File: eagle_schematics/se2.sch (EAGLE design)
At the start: 2 parts

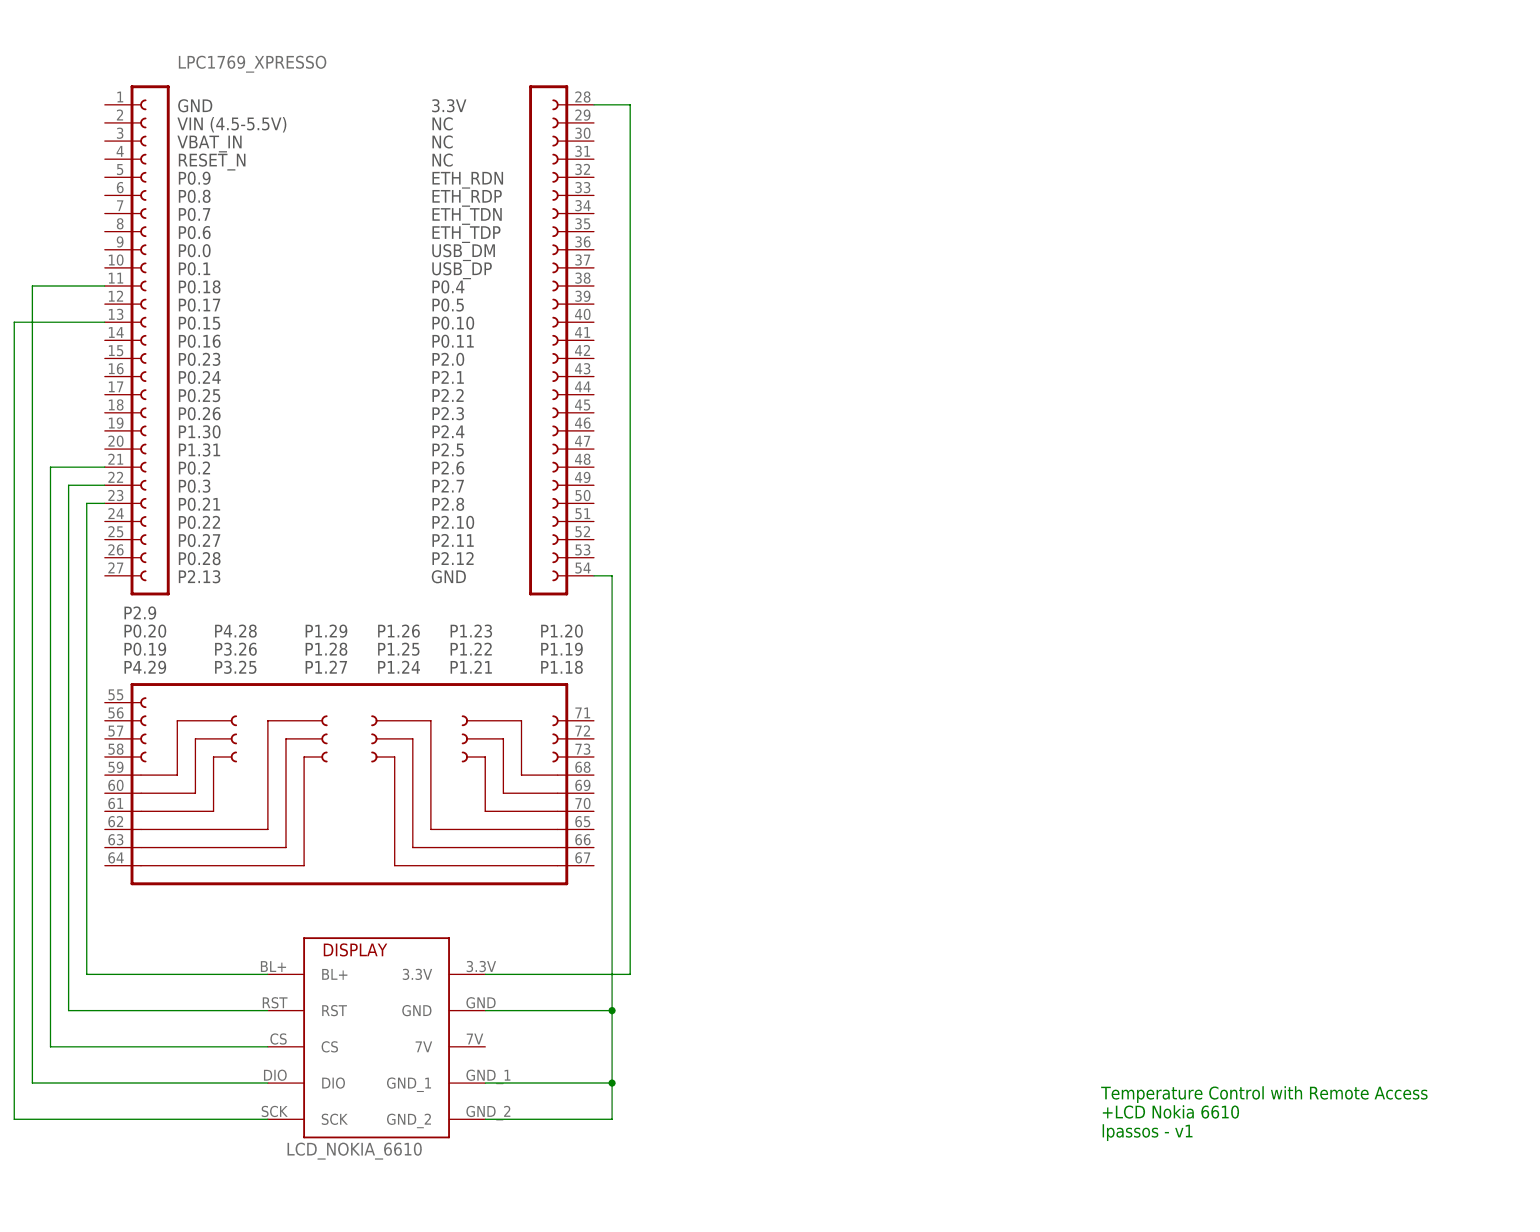
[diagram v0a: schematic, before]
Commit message: Thermometer added
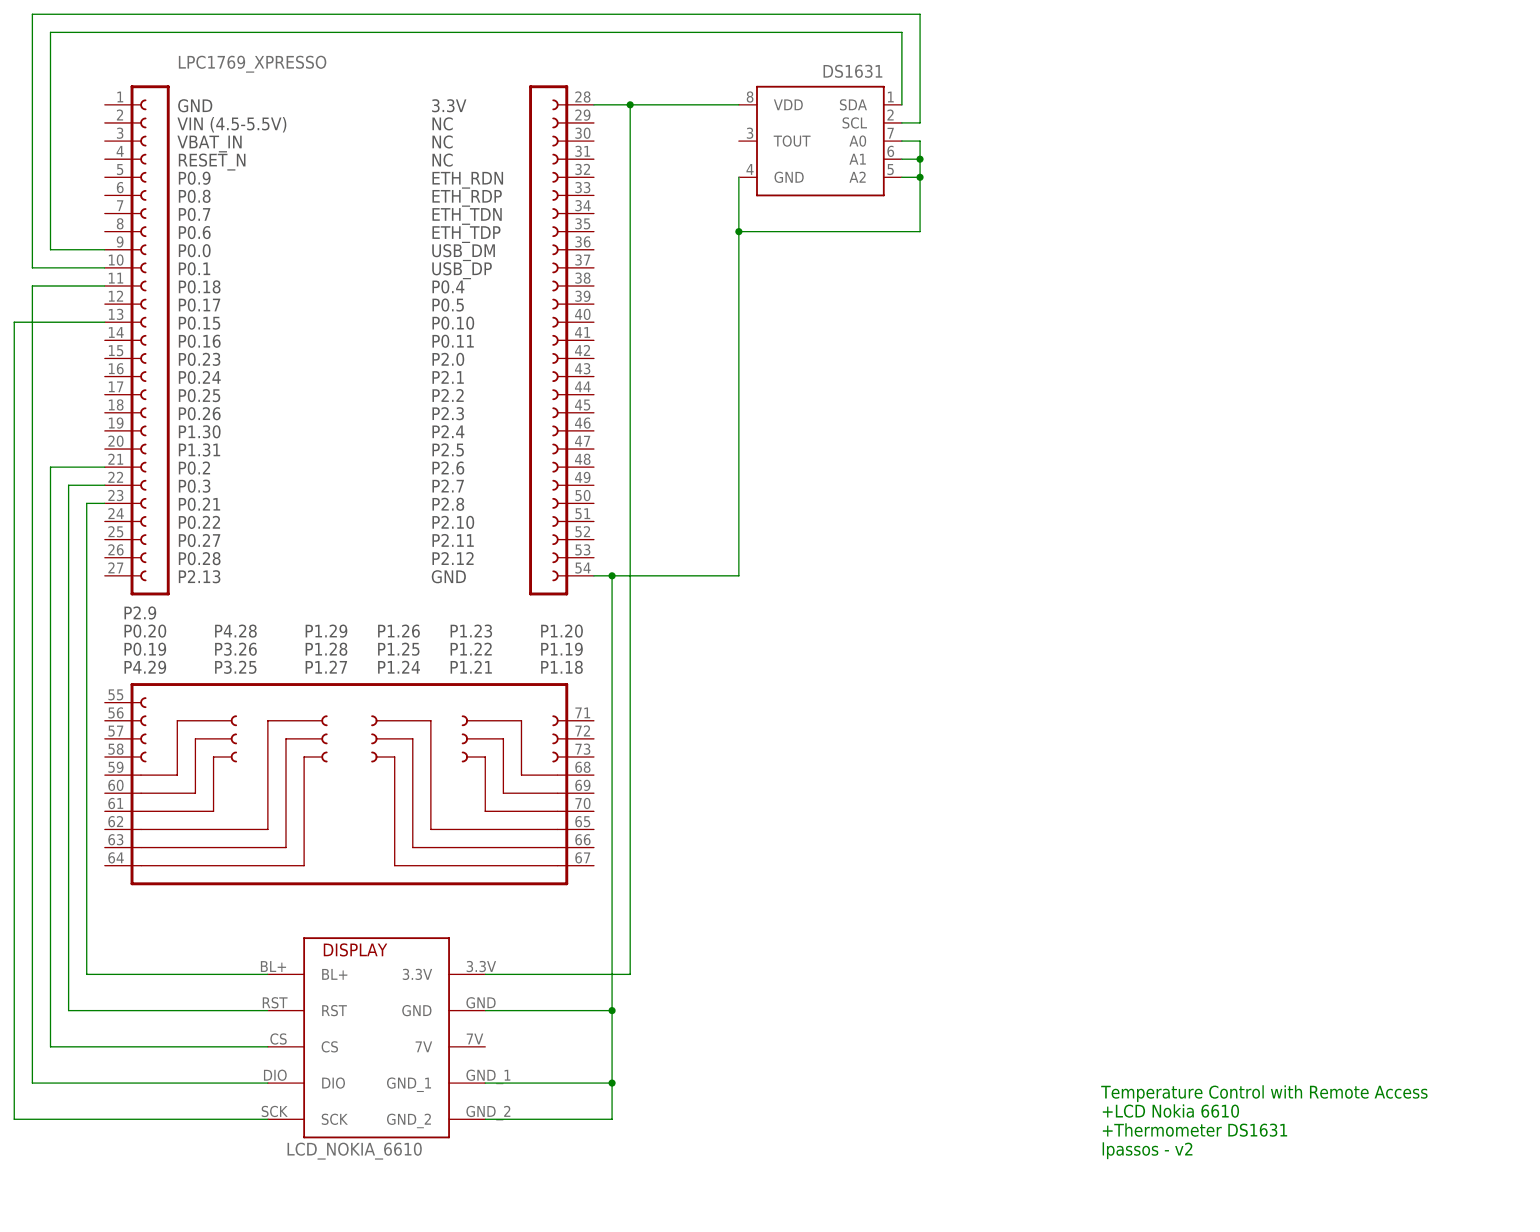
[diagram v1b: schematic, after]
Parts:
- added DS1631: DS1621, maxim:DS1621
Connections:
- removed net N$1: DISPLAY.GND, DISPLAY.GND_1, DISPLAY.GND_2, LPC1769_XPRESSO.54
- new net N$10: DS1631.SDA, LPC1769_XPRESSO.9
- new net N$11: DS1631.SCL, LPC1769_XPRESSO.10
- new net N$9: DISPLAY.GND, DISPLAY.GND_1, DISPLAY.GND_2, DS1631.A0, DS1631.A1, DS1631.A2, DS1631.GND, LPC1769_XPRESSO.54
- net N$3: now also DS1631.VDD
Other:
- note added: "Temperature Control with Remote Access +LCD Nokia 6610 +Thermometer DS1631 lpassos - v2"
- note removed: "Temperature Control with Remote Access +LCD Nokia 6610 lpassos - v1"
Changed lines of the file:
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@@
 <setting verticaltext="up"/>
 </settings>
-<grid distance="0.1" unitdist="inch" unit="inch" style="lines" multiple="1" display="no" altdistance="0.01" altunitdist="inch" altunit="inch"/>
+<grid distance="0.1" unitdist="inch" unit="inch" style="lines" multiple="1" display="yes" altdistance="0.01" altunitdist="inch" altunit="inch"/>
 <layers>
 <layer number="1" name="Top" color="4" fill="1" visible="no" active="no"/>
@@
 <part name="FRAME1" library="frames" deviceset="A4L-LOC" device=""/>
 <part name="DISPLAY" library="nokia_lcd6610" deviceset="NOKIA_LCD_6610" device=""/>
+<part name="DS1631" library="maxim" deviceset="DS1621" device=""/>
 </parts>
 <sheets>
 <sheet>
 <plain>
-<text x="182.88" y="99.06" size="1.778" layer="91">Temperature Control with Remote Access
+<text x="182.88" y="96.52" size="1.778" layer="91">Temperature Control with Remote Access
 +LCD Nokia 6610
-lpassos - v1</text>
++Thermometer DS1631
+lpassos - v2</text>
 </plain>
 <instances>
@@
 <attribute name="NAME" x="73.66" y="124.46" size="1.778" layer="94"/>
 </instance>
+<instance part="DS1631" gate="G$1" x="144.78" y="238.76" smashed="yes" rot="MR0">
+<attribute name="MPN" x="144.78" y="238.76" size="1.778" layer="96" rot="MR0" display="off"/>
+<attribute name="NAME" x="152.4" y="247.65" size="1.778" layer="95" rot="MR0"/>
+</instance>
 </instances>
 <busses>
 </busses>
 <nets>
-<net name="N$1" class="0">
+<net name="N$3" class="0">
+<segment>
+<pinref part="LPC1769_XPRESSO" gate="G$1" pin="28"/>
+<wire x1="111.76" y1="243.84" x2="116.84" y2="243.84" width="0.1524" layer="91"/>
+<wire x1="116.84" y1="243.84" x2="116.84" y2="121.92" width="0.1524" layer="91"/>
+<pinref part="DISPLAY" gate="G$1" pin="3.3V"/>
+<wire x1="116.84" y1="121.92" x2="96.52" y2="121.92" width="0.1524" layer="91"/>
+<pinref part="DS1631" gate="G$1" pin="VDD"/>
+<wire x1="132.08" y1="243.84" x2="116.84" y2="243.84" width="0.1524" layer="91"/>
+<junction x="116.84" y="243.84"/>
+</segment>
+</net>
+<net name="N$4" class="0">
+<segment>
+<pinref part="LPC1769_XPRESSO" gate="G$1" pin="23"/>
+<wire x1="43.18" y1="187.96" x2="40.64" y2="187.96" width="0.1524" layer="91"/>
+<wire x1="40.64" y1="187.96" x2="40.64" y2="121.92" width="0.1524" layer="91"/>
+<pinref part="DISPLAY" gate="G$1" pin="BL+"/>
+<wire x1="40.64" y1="121.92" x2="66.04" y2="121.92" width="0.1524" layer="91"/>
+</segment>
+</net>
+<net name="N$5" class="0">
+<segment>
+<pinref part="LPC1769_XPRESSO" gate="G$1" pin="22"/>
+<wire x1="43.18" y1="190.5" x2="38.1" y2="190.5" width="0.1524" layer="91"/>
+<wire x1="38.1" y1="190.5" x2="38.1" y2="116.84" width="0.1524" layer="91"/>
+<pinref part="DISPLAY" gate="G$1" pin="RST"/>
+<wire x1="38.1" y1="116.84" x2="66.04" y2="116.84" width="0.1524" layer="91"/>
+</segment>
+</net>
+<net name="N$6" class="0">
+<segment>
+<pinref part="LPC1769_XPRESSO" gate="G$1" pin="21"/>
+<wire x1="43.18" y1="193.04" x2="35.56" y2="193.04" width="0.1524" layer="91"/>
+<wire x1="35.56" y1="193.04" x2="35.56" y2="111.76" width="0.1524" layer="91"/>
+<pinref part="DISPLAY" gate="G$1" pin="CS"/>
+<wire x1="35.56" y1="111.76" x2="66.04" y2="111.76" width="0.1524" layer="91"/>
+</segment>
+</net>
+<net name="N$7" class="0">
+<segment>
+<pinref part="LPC1769_XPRESSO" gate="G$1" pin="11"/>
+<wire x1="43.18" y1="218.44" x2="33.02" y2="218.44" width="0.1524" layer="91"/>
+<wire x1="33.02" y1="218.44" x2="33.02" y2="106.68" width="0.1524" layer="91"/>
+<pinref part="DISPLAY" gate="G$1" pin="DIO"/>
+<wire x1="33.02" y1="106.68" x2="66.04" y2="106.68" width="0.1524" layer="91"/>
+</segment>
+</net>
+<net name="N$8" class="0">
+<segment>
+<pinref part="LPC1769_XPRESSO" gate="G$1" pin="13"/>
+<wire x1="43.18" y1="213.36" x2="30.48" y2="213.36" width="0.1524" layer="91"/>
+<wire x1="30.48" y1="213.36" x2="30.48" y2="101.6" width="0.1524" layer="91"/>
+<pinref part="DISPLAY" gate="G$1" pin="SCK"/>
+<wire x1="30.48" y1="101.6" x2="66.04" y2="101.6" width="0.1524" layer="91"/>
+</segment>
+</net>
+<net name="N$9" class="0">
 <segment>
 <pinref part="DISPLAY" gate="G$1" pin="GND"/>
@@
 <junction x="114.3" y="116.84"/>
 <junction x="114.3" y="106.68"/>
-</segment>
-</net>
-<net name="N$3" class="0">
-<segment>
-<pinref part="LPC1769_XPRESSO" gate="G$1" pin="28"/>
-<wire x1="111.76" y1="243.84" x2="116.84" y2="243.84" width="0.1524" layer="91"/>
-<wire x1="116.84" y1="243.84" x2="116.84" y2="121.92" width="0.1524" layer="91"/>
-<pinref part="DISPLAY" gate="G$1" pin="3.3V"/>
-<wire x1="116.84" y1="121.92" x2="96.52" y2="121.92" width="0.1524" layer="91"/>
-</segment>
-</net>
-<net name="N$4" class="0">
-<segment>
-<pinref part="LPC1769_XPRESSO" gate="G$1" pin="23"/>
-<wire x1="43.18" y1="187.96" x2="40.64" y2="187.96" width="0.1524" layer="91"/>
-<wire x1="40.64" y1="187.96" x2="40.64" y2="121.92" width="0.1524" layer="91"/>
-<pinref part="DISPLAY" gate="G$1" pin="BL+"/>
-<wire x1="40.64" y1="121.92" x2="66.04" y2="121.92" width="0.1524" layer="91"/>
-</segment>
-</net>
-<net name="N$5" class="0">
-<segment>
-<pinref part="LPC1769_XPRESSO" gate="G$1" pin="22"/>
-<wire x1="43.18" y1="190.5" x2="38.1" y2="190.5" width="0.1524" layer="91"/>
-<wire x1="38.1" y1="190.5" x2="38.1" y2="116.84" width="0.1524" layer="91"/>
-<pinref part="DISPLAY" gate="G$1" pin="RST"/>
-<wire x1="38.1" y1="116.84" x2="66.04" y2="116.84" width="0.1524" layer="91"/>
-</segment>
-</net>
-<net name="N$6" class="0">
-<segment>
-<pinref part="LPC1769_XPRESSO" gate="G$1" pin="21"/>
-<wire x1="43.18" y1="193.04" x2="35.56" y2="193.04" width="0.1524" layer="91"/>
-<wire x1="35.56" y1="193.04" x2="35.56" y2="111.76" width="0.1524" layer="91"/>
-<pinref part="DISPLAY" gate="G$1" pin="CS"/>
-<wire x1="35.56" y1="111.76" x2="66.04" y2="111.76" width="0.1524" layer="91"/>
-</segment>
-</net>
-<net name="N$7" class="0">
-<segment>
-<pinref part="LPC1769_XPRESSO" gate="G$1" pin="11"/>
-<wire x1="43.18" y1="218.44" x2="33.02" y2="218.44" width="0.1524" layer="91"/>
-<wire x1="33.02" y1="218.44" x2="33.02" y2="106.68" width="0.1524" layer="91"/>
-<pinref part="DISPLAY" gate="G$1" pin="DIO"/>
-<wire x1="33.02" y1="106.68" x2="66.04" y2="106.68" width="0.1524" layer="91"/>
-</segment>
-</net>
-<net name="N$8" class="0">
-<segment>
-<pinref part="LPC1769_XPRESSO" gate="G$1" pin="13"/>
-<wire x1="43.18" y1="213.36" x2="30.48" y2="213.36" width="0.1524" layer="91"/>
-<wire x1="30.48" y1="213.36" x2="30.48" y2="101.6" width="0.1524" layer="91"/>
-<pinref part="DISPLAY" gate="G$1" pin="SCK"/>
-<wire x1="30.48" y1="101.6" x2="66.04" y2="101.6" width="0.1524" layer="91"/>
-</segment>
-</net>
+<wire x1="132.08" y1="226.06" x2="132.08" y2="177.8" width="0.1524" layer="91"/>
+<wire x1="132.08" y1="177.8" x2="114.3" y2="177.8" width="0.1524" layer="91"/>
+<junction x="114.3" y="177.8"/>
+<wire x1="132.08" y1="226.06" x2="157.48" y2="226.06" width="0.1524" layer="91"/>
+<pinref part="DS1631" gate="G$1" pin="A2"/>
+<wire x1="154.94" y1="233.68" x2="157.48" y2="233.68" width="0.1524" layer="91"/>
+<wire x1="157.48" y1="233.68" x2="157.48" y2="236.22" width="0.1524" layer="91"/>
+<pinref part="DS1631" gate="G$1" pin="A1"/>
+<wire x1="154.94" y1="236.22" x2="157.48" y2="236.22" width="0.1524" layer="91"/>
+<wire x1="157.48" y1="236.22" x2="157.48" y2="238.76" width="0.1524" layer="91"/>
+<pinref part="DS1631" gate="G$1" pin="A0"/>
+<wire x1="157.48" y1="238.76" x2="154.94" y2="238.76" width="0.1524" layer="91"/>
+<junction x="157.48" y="236.22"/>
+<wire x1="157.48" y1="226.06" x2="157.48" y2="233.68" width="0.1524" layer="91"/>
+<junction x="157.48" y="233.68"/>
+<pinref part="DS1631" gate="G$1" pin="GND"/>
+<wire x1="132.08" y1="233.68" x2="132.08" y2="226.06" width="0.1524" layer="91"/>
+<junction x="132.08" y="226.06"/>
+</segment>
+</net>
+<net name="N$10" class="0">
+<segment>
+<pinref part="LPC1769_XPRESSO" gate="G$1" pin="9"/>
+<wire x1="43.18" y1="223.52" x2="35.56" y2="223.52" width="0.1524" layer="91"/>
+<wire x1="35.56" y1="223.52" x2="35.56" y2="254" width="0.1524" layer="91"/>
+<pinref part="DS1631" gate="G$1" pin="SDA"/>
+<wire x1="35.56" y1="254" x2="154.94" y2="254" width="0.1524" layer="91"/>
+<wire x1="154.94" y1="254" x2="154.94" y2="243.84" width="0.1524" layer="91"/>
+</segment>
+</net>
+<net name="N$11" class="0">
+<segment>
+<pinref part="LPC1769_XPRESSO" gate="G$1" pin="10"/>
+<wire x1="43.18" y1="220.98" x2="33.02" y2="220.98" width="0.1524" layer="91"/>
+<wire x1="33.02" y1="220.98" x2="33.02" y2="256.54" width="0.1524" layer="91"/>
+<wire x1="33.02" y1="256.54" x2="157.48" y2="256.54" width="0.1524" layer="91"/>
+<wire x1="157.48" y1="256.54" x2="157.48" y2="241.3" width="0.1524" layer="91"/>
+<pinref part="DS1631" gate="G$1" pin="SCL"/>
+<wire x1="157.48" y1="241.3" x2="154.94" y2="241.3" width="0.1524" layer="91"/>
+</segment>
+</net>

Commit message: Mag_jack added
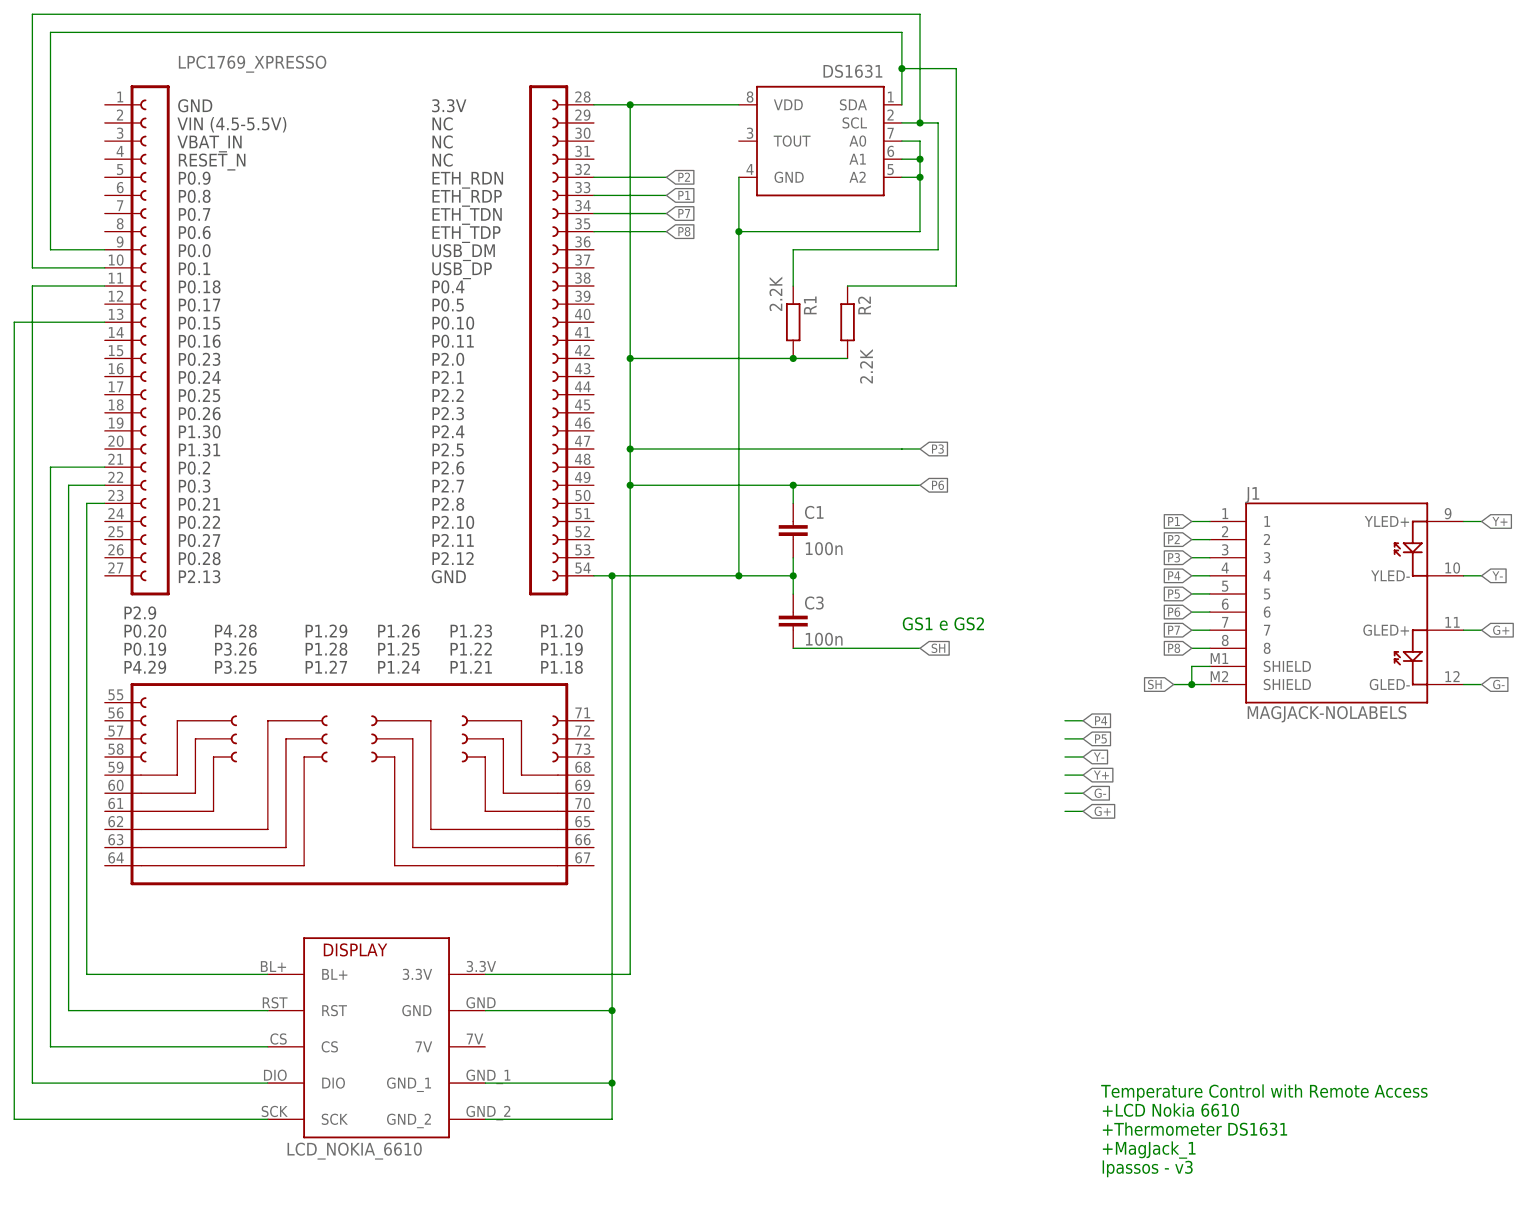
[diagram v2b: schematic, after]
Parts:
- added C1, C3: 100n, capacitor-wima:C2,5-3
- added J1: MAGJACK-NOLABELS, SparkFun-Connectors:MAGJACK-NOLABELS
- added R1, R2: 2.2K, eagle-ltspice:R
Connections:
- removed net N$3: DISPLAY.3.3V, DS1631.VDD, LPC1769_XPRESSO.28
- new net G+: J1.GLED+
- new net G-: J1.GLED-
- new net P1: J1.1, LPC1769_XPRESSO.33
- new net P2: J1.2, LPC1769_XPRESSO.32
- new net P3: J1.3
- new net P4: J1.4
- new net P5: J1.5
- new net P6: C1.1, DISPLAY.3.3V, DS1631.VDD, J1.6, LPC1769_XPRESSO.28, R1.2, R2.2
- new net P7: J1.7, LPC1769_XPRESSO.34
- new net P8: J1.8, LPC1769_XPRESSO.35
- new net SH: C3.2, J1.SHIELD@0, J1.SHIELD@1
- new net Y+: J1.YLED+
- new net Y-: J1.YLED-
- net N$10: now also R2.1
- net N$11: now also R1.1
- net N$9: now also C1.2, C3.1
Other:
- note added: "GS1 e GS2"
- note added: "Temperature Control with Remote Access +LCD Nokia 6610 +Thermometer DS1631 +MagJack_1 lpassos - v3"
- note removed: "Temperature Control with Remote Access +LCD Nokia 6610 +Thermometer DS1631 lpassos - v2"
